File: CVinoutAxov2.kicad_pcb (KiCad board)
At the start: 2 copper layers, 108 x 109.2 mm, 71 parts, among them J1 CVin A, J10 audio_in L, J11 audio_in R, J12 Conn_01x04, J13 audio_out L, J14 audio_out R, J15 USB_A, J16 Conn_01x04, J17 Conn_01x02, J2 CVin B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

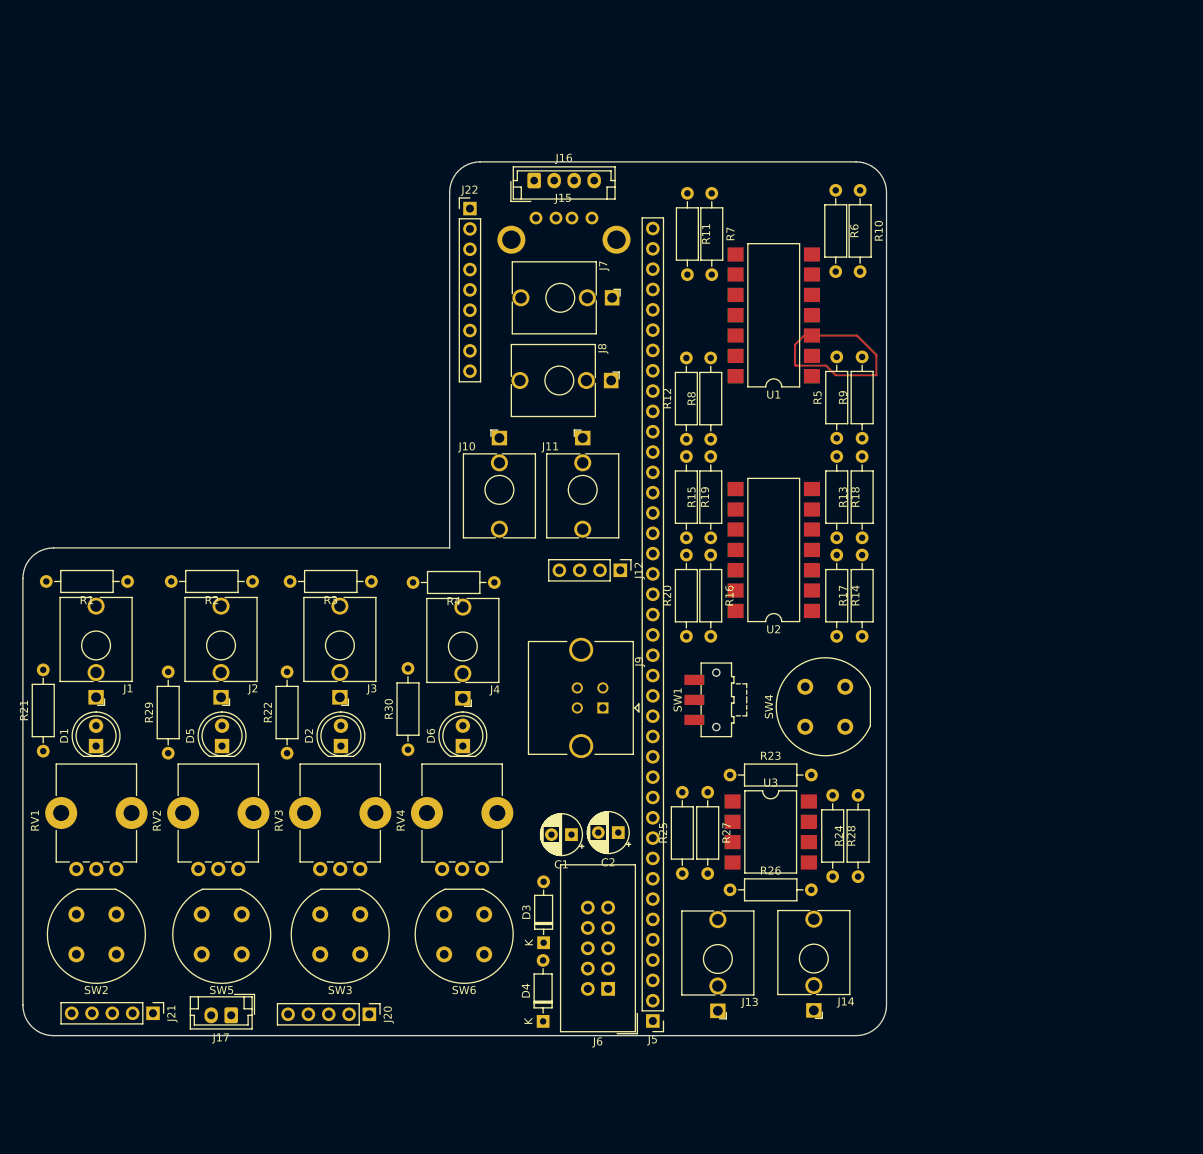
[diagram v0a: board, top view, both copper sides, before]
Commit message: added disc caps
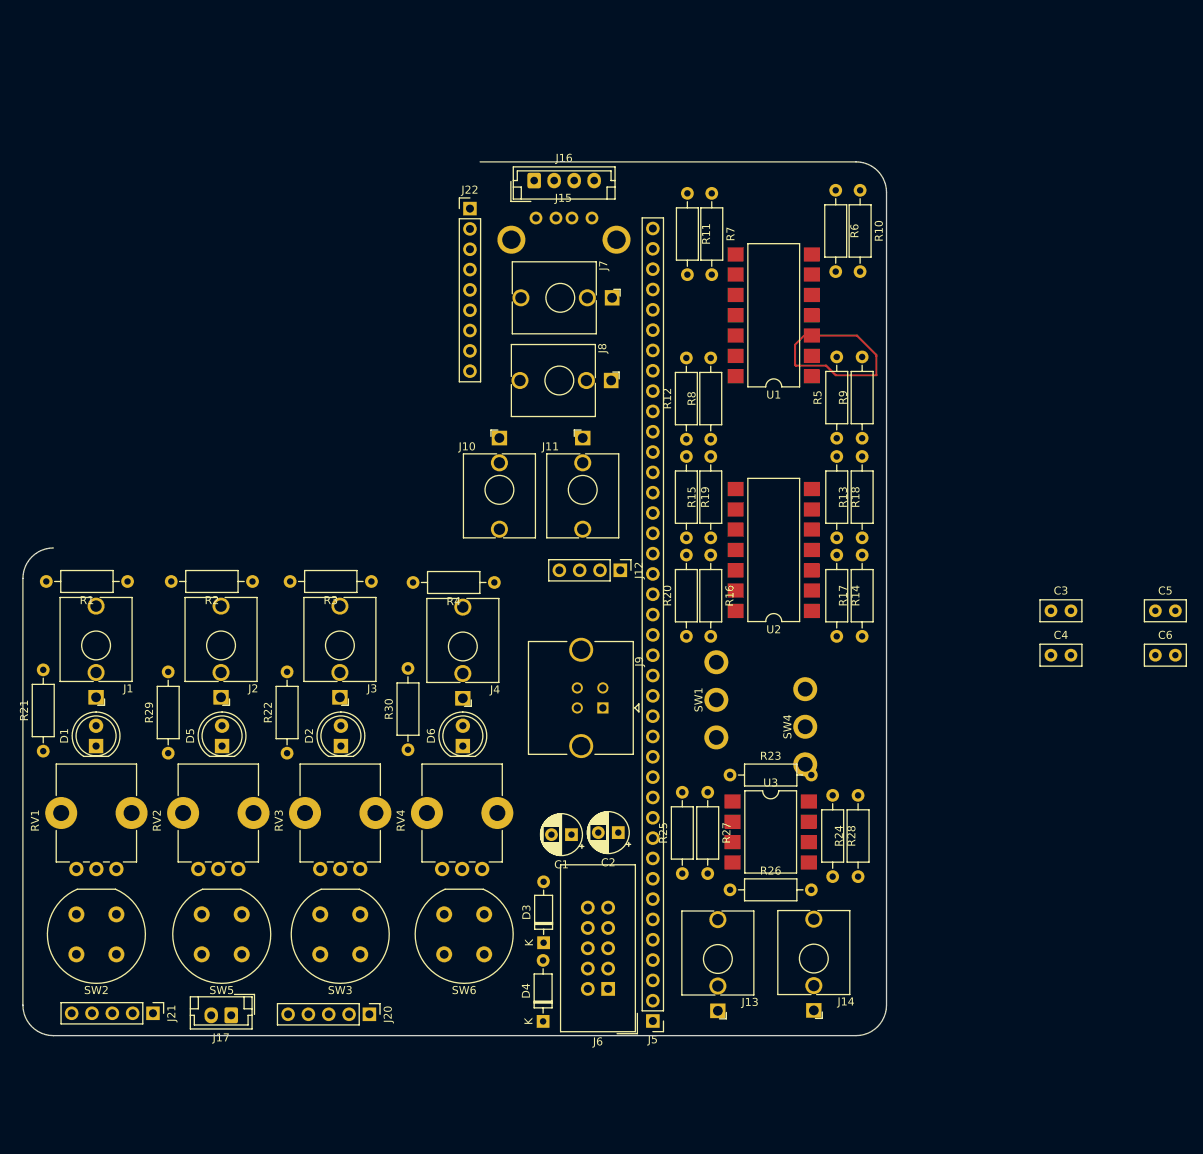
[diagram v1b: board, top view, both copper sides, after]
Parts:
- added C3: C_Small, Capacitor_THT:C_Disc_D5.0mm_W2.5mm_P2.50mm, F.Cu at (159.0, 105.6)
- added C4: C_Small, Capacitor_THT:C_Disc_D5.0mm_W2.5mm_P2.50mm, F.Cu at (159.0, 111.2)
- added C5: C_Small, Capacitor_THT:C_Disc_D5.0mm_W2.5mm_P2.50mm, F.Cu at (172.0, 105.6)
- added C6: C_Small, Capacitor_THT:C_Disc_D5.0mm_W2.5mm_P2.50mm, F.Cu at (172.0, 111.2)
- SW1: footprint Button_Switch_SMD:SW_SPDT_CK-JS102011SAQN -> Button_Switch_THT:E-switch_SPDT_100SP1T1B4M2QE
- SW4: footprint Button_Switch_THT:Push_E-Switch_KS01Q01 -> Button_Switch_THT:E-switch_SPDT_100SP1T1B4M2QE
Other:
- outline, holes or cut-outs redrawn

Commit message: added disc caps
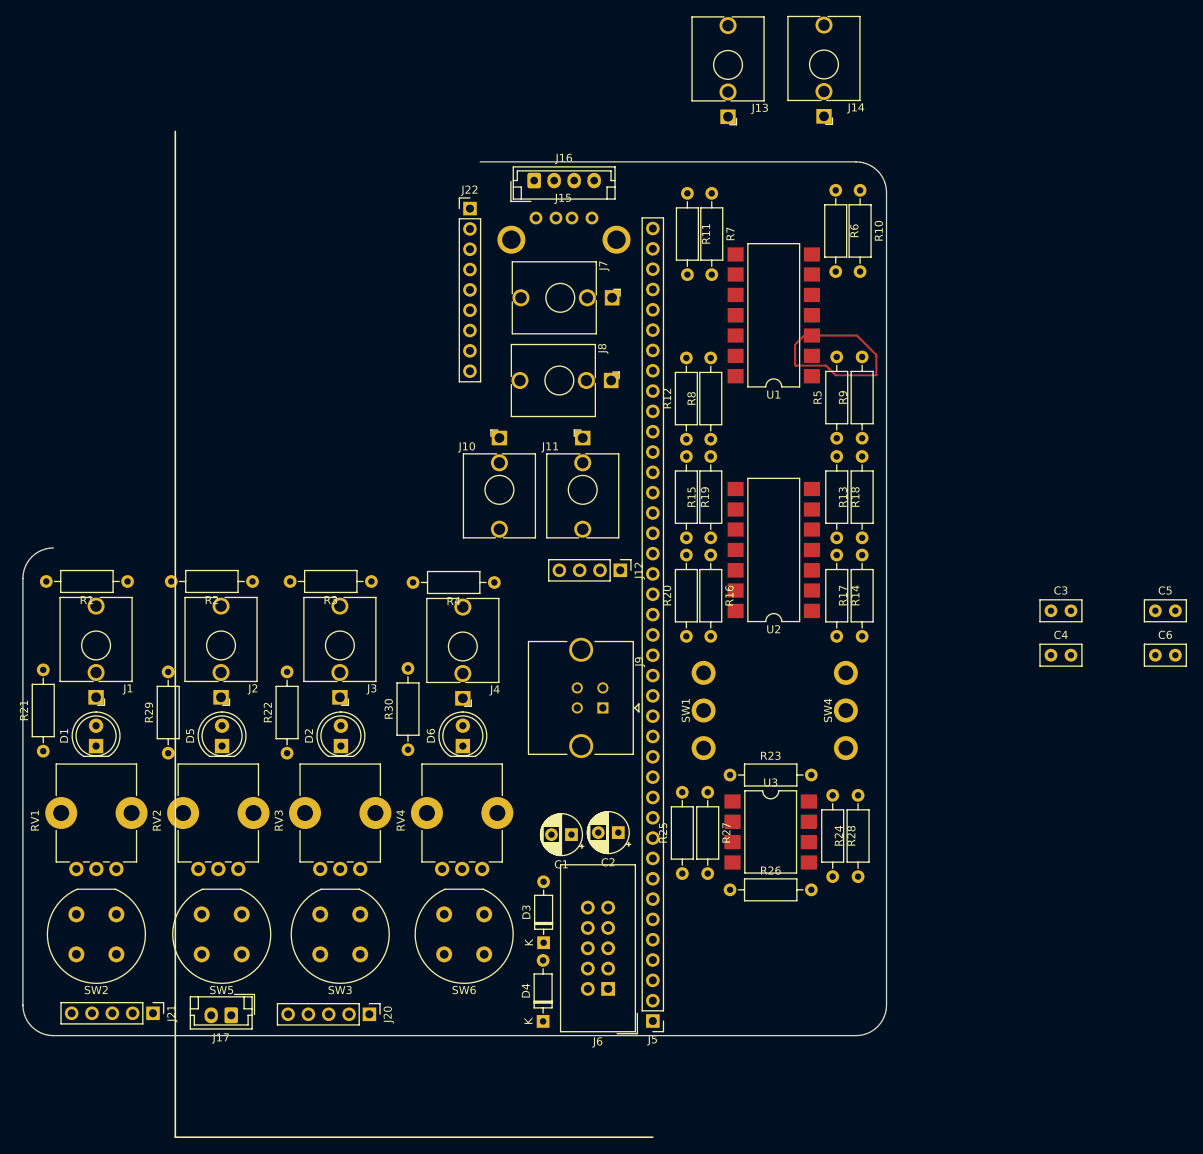
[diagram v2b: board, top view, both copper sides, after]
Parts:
- moved J14 111.8 mm to (130.6, 43.8)
- moved J13 111.8 mm to (118.6, 43.9)
- moved SW4 5.47 mm to (133.3, 118.1)
- moved SW1 2.07 mm to (115.6, 118.1)
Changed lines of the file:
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@@
   (general
     (thickness 1.6)
-    (drawings 2520)
+    (drawings 2522)
     (tracks 10)
     (zones 0)
@@
     (38 B.Mask user)
     (39 F.Mask user)
-    (40 Dwgs.User user hide)
+    (40 Dwgs.User user)
     (41 Cmts.User user)
     (42 Eco1.User user)
@@
     (solder_mask_min_width 0.25)
     (aux_axis_origin 0 0)
-    (visible_elements FFFFFF7F)
+    (visible_elements FFFFF77F)
     (pcbplotparams
       (layerselection 0x010fc_ffffffff)
@@
   )
   (module Connector_Audio:Jack_3.5mm_QingPu_WQP-PJ398SM_Vertical_CircularHoles (layer F.Cu)
-    (at 117.348 155.6512 180)
+    (at 118.618 43.8912 180)
     (descr "TRS 3.5mm, vertical, Thonkiconn, PCB mount, (http://www.qingpu-electronics.com/en/products/WQP-PJ398SM-362.html)")
     (tags "WQP-PJ398SM WQP-PJ301M-12 TRS 3.5mm mono vertical jack thonkiconn qingpu")
@@
   )
   (module Connector_Audio:Jack_3.5mm_QingPu_WQP-PJ398SM_Vertical_CircularHoles (layer F.Cu)
-    (at 129.343311 155.596604 180)
+    (at 130.613311 43.836604 180)
     (descr "TRS 3.5mm, vertical, Thonkiconn, PCB mount, (http://www.qingpu-electronics.com/en/products/WQP-PJ398SM-362.html)")
     (tags "WQP-PJ398SM WQP-PJ301M-12 TRS 3.5mm mono vertical jack thonkiconn qingpu")
@@
   )
   (module Button_Switch_THT:E-switch_SPDT_100SP1T1B4M2QE (layer F.Cu)
-    (at 117.1575 116.7765 90)
+    (at 115.57 118.11 90)
     (fp_text reference SW1 (at 0 -2.2 90) (layer F.SilkS)
       (effects (font (size 1 1) (thickness 0.15)))
@@
   )
   (module Button_Switch_THT:E-switch_SPDT_100SP1T1B4M2QE (layer F.Cu)
-    (at 128.27 120.142 90)
+    (at 133.35 118.11 90)
     (fp_text reference SW4 (at 0 -2.2 90) (layer F.SilkS)
       (effects (font (size 1 1) (thickness 0.15)))
@@
     )
   )
+  (gr_line (start 49.53 171.45) (end 49.53 45.72) (layer F.SilkS) (width 0.2))
+  (gr_line (start 109.22 171.45) (end 49.53 171.45) (layer F.SilkS) (width 0.2))
   (gr_arc (start 34.29 101.6) (end 34.29 97.79) (angle -90) (layer Edge.Cuts) (width 0.1))
   (gr_arc (start 34.29 154.94) (end 30.48 154.94) (angle -90) (layer Edge.Cuts) (width 0.1))
